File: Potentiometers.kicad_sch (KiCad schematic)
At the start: 10 parts, among them J7 Conn_01x03, J9 Conn_01x03

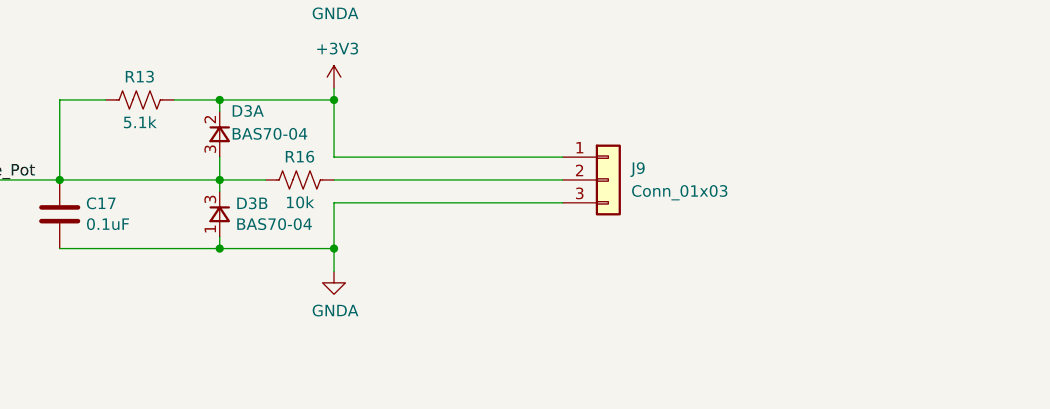
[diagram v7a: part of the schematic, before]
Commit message: added circuitry for limit switch brake, added mosfet to drive LEDs, cleaned up legacy comments, updated resistor values for LEDs
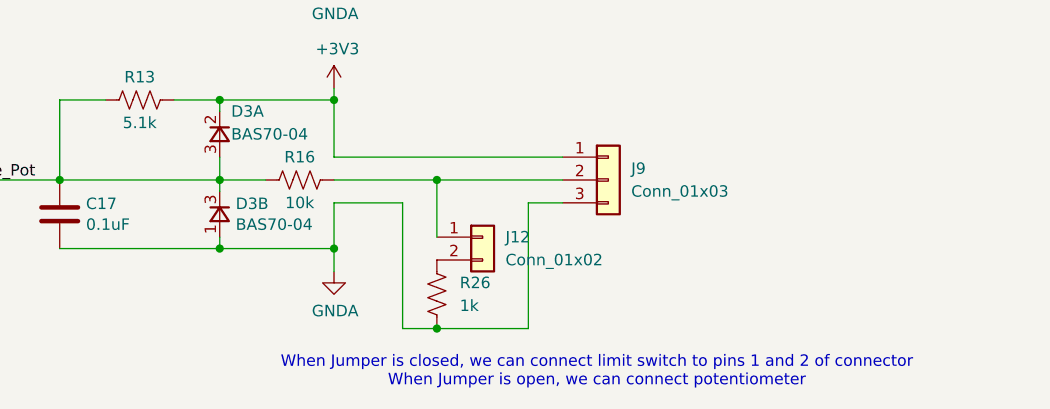
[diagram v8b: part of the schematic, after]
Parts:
- added J12: Conn_01x02, Connector_PinHeader_2.54mm:PinHeader_1x02_P2.54mm_Vertical, symbol Connector_Generic:Conn_01x02
- added R26: 1k, symbol Device:R_US
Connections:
- net GNDA: now also R26.2
- net at J9.2 (Pin_2), R16.1: now also J12.1 (Pin_1)
- new net: J12.2 (Pin_2), R26.1
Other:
- note added: "When Jumper is closed, we can connect limit switch to pins 1 and 2 of connector When Jumper is open, we can connect potentiometer"
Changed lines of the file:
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@@
+	)
+	(junction
+		(at 125.73 113.03)
+		(diameter 0)
+		(color 0 0 0 0)
 	)
 	(junction
@@
 	)
 	(junction
+		(at 125.73 129.54)
+		(diameter 0)
+		(color 0 0 0 0)
+	)
+	(junction
 		(at 101.6 104.14)
 		(diameter 0)
@@
 	(wire
 		(pts
+			(xy 125.73 113.03) (xy 125.73 119.38)
+		)
+		(stroke
+			(width 0)
+			(type default)
+		)
+	)
+	(wire
+		(pts
 			(xy 114.3 102.87) (xy 114.3 104.14)
 		)
@@
 	(wire
 		(pts
+			(xy 125.73 113.03) (xy 139.7 113.03)
+		)
+		(stroke
+			(width 0)
+			(type default)
+		)
+	)
+	(wire
+		(pts
+			(xy 114.3 115.57) (xy 121.92 115.57)
+		)
+		(stroke
+			(width 0)
+			(type default)
+		)
+	)
+	(wire
+		(pts
 			(xy 114.3 71.12) (xy 114.3 77.47)
 		)
@@
 	(wire
 		(pts
-			(xy 114.3 113.03) (xy 139.7 113.03)
+			(xy 114.3 113.03) (xy 125.73 113.03)
 		)
 		(stroke
@@
 	(wire
 		(pts
-			(xy 114.3 115.57) (xy 139.7 115.57)
-		)
-		(stroke
-			(width 0)
-			(type default)
-		)
-	)
-	(wire
-		(pts
 			(xy 101.6 81.28) (xy 101.6 80.01)
 		)
@@
 	(wire
 		(pts
+			(xy 121.92 129.54) (xy 125.73 129.54)
+		)
+		(stroke
+			(width 0)
+			(type default)
+		)
+	)
+	(wire
+		(pts
+			(xy 139.7 115.57) (xy 135.89 115.57)
+		)
+		(stroke
+			(width 0)
+			(type default)
+		)
+	)
+	(wire
+		(pts
 			(xy 114.3 82.55) (xy 139.7 82.55)
 		)
@@
 	(wire
 		(pts
+			(xy 121.92 115.57) (xy 121.92 129.54)
+		)
+		(stroke
+			(width 0)
+			(type default)
+		)
+	)
+	(wire
+		(pts
 			(xy 114.3 110.49) (xy 139.7 110.49)
 		)
@@
 	(wire
 		(pts
+			(xy 135.89 115.57) (xy 135.89 129.54)
+		)
+		(stroke
+			(width 0)
+			(type default)
+		)
+	)
+	(wire
+		(pts
 			(xy 114.3 90.17) (xy 114.3 87.63)
 		)
@@
 			(width 0)
 			(type default)
+		)
+	)
+	(wire
+		(pts
+			(xy 135.89 129.54) (xy 125.73 129.54)
+		)
+		(stroke
+			(width 0)
+			(type default)
+		)
+	)
+	(text "When Jumper is closed, we can connect limit switch to pins 1 and 2 of connector\nWhen Jumper is open, we can connect potentiometer\n"
+		(exclude_from_sim no)
+		(at 143.51 134.366 0)
+		(effects
+			(font
+				(size 1.27 1.27)
+				(color 255 5 21 1)
+			)
 		)
 	)
@@
 					(unit 1)
 				)
+			)
+		)
+	)
+	(symbol
+		(lib_id "Device:R_US")
+		(at 125.73 125.73 0)
+		(unit 1)
+		(exclude_from_sim no)
+		(in_bom yes)
+		(on_board yes)
+		(dnp no)
+		(fields_autoplaced yes)
+		(property "Reference" "R26"
+			(at 128.27 124.4599 0)
+			(effects
+				(font
+					(size 1.27 1.27)
+				)
+				(justify left)
+			)
+		)
+		(property "Value" "1k"
+			(at 128.27 126.9999 0)
+			(effects
+				(font
+					(size 1.27 1.27)
+				)
+				(justify left)
+			)
+		)
+		(property "Footprint" ""
+			(at 126.746 125.984 90)
+			(effects
+				(font
+					(size 1.27 1.27)
+				)
+				(hide yes)
+			)
+		)
+		(property "Datasheet" "~"
+			(at 125.73 125.73 0)
+			(effects
+				(font
+					(size 1.27 1.27)
+				)
+				(hide yes)
+			)
+		)
+		(property "Description" "Resistor, US symbol"
+			(at 125.73 125.73 0)
+			(effects
+				(font
+					(size 1.27 1.27)
+				)
+				(hide yes)
+			)
+		)
+		(pin "2"
+		)
+		(pin "1"
+		)
+		(instances
+			(project ""
+				(path "/66218487-e316-4467-9eba-79d4626ab24e/00000000-0000-0000-0000-00005fa99dc3"
+					(reference "R26")
+					(unit 1)
+				)
+			)
+		)
+	)
+	(symbol
+		(lib_id "Connector_Generic:Conn_01x02")
+		(at 130.81 119.38 0)
+		(unit 1)
+		(exclude_from_sim no)
+		(in_bom yes)
+		(on_board yes)
+		(dnp no)
+		(fields_autoplaced yes)
+		(property "Reference" "J12"
+			(at 133.35 119.3799 0)
+			(effects
+				(font
+					(size 1.27 1.27)
+				)
+				(justify left)
+			)
+		)
+		(property "Value" "Conn_01x02"
+			(at 133.35 121.9199 0)
+			(effects
+				(font
+					(size 1.27 1.27)
+				)
+				(justify left)
+			)
+		)
+		(property "Footprint" "Connector_PinHeader_2.54mm:PinHeader_1x02_P2.54mm_Vertical"
+			(at 130.81 119.38 0)
+			(effects
+				(font
+					(size 1.27 1.27)
+				)
+				(hide yes)
+			)
+		)
+		(property "Datasheet" "~"
+			(at 130.81 119.38 0)
+			(effects
+				(font
+					(size 1.27 1.27)
+				)
+				(hide yes)
+			)
+		)
+		(property "Description" "Generic connector, single row, 01x02, script generated (kicad-library-utils/schlib/autogen/connector/)"
+			(at 130.81 119.38 0)
+			(effects
+				(font
+					(size 1.27 1.27)
+				)
+				(hide yes)
+			)
+		)
+		(pin "1"
+		)
+		(pin "2"
+		)
+		(instances
+			(project ""
+				(path "/66218487-e316-4467-9eba-79d4626ab24e/00000000-0000-0000-0000-00005fa99dc3"
+					(reference "J12")
+					(unit 1)
+				)
